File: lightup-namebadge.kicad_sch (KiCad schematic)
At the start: 22 parts, among them Q1 PNP, Q2 NPN, Q3 NPN, Q4 NPN, Q5 NPN, SW1 SW_Push, SW2 SW_Push

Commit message: fix: disconnect pin 3 of RV1 from VSS to save power
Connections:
- net VSS: no longer RV1.3
- no-connect marks 0 -> 1
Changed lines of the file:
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@@
-	)
-	(junction
-		(at 72.39 82.55)
-		(diameter 0)
-		(color 0 0 0 0)
 	)
 	(junction
@@
 	)
 	(junction
+		(at 135.89 92.71)
+		(diameter 0)
+		(color 0 0 0 0)
+	)
+	(junction
+		(at 153.67 82.55)
+		(diameter 0)
+		(color 0 0 0 0)
+	)
+	(junction
+		(at 196.85 90.17)
+		(diameter 0)
+		(color 0 0 0 0)
+	)
+	(junction
+		(at 176.53 90.17)
+		(diameter 0)
+		(color 0 0 0 0)
+	)
+	(junction
 		(at 107.95 121.92)
 		(diameter 0)
 		(color 0 0 0 0)
 	)
-	(junction
-		(at 135.89 92.71)
-		(diameter 0)
-		(color 0 0 0 0)
-	)
-	(junction
-		(at 153.67 82.55)
-		(diameter 0)
-		(color 0 0 0 0)
-	)
-	(junction
-		(at 196.85 90.17)
-		(diameter 0)
-		(color 0 0 0 0)
-	)
-	(junction
-		(at 176.53 90.17)
-		(diameter 0)
-		(color 0 0 0 0)
+	(no_connect
+		(at 88.9 82.55)
 	)
 	(wire
@@
 	(wire
 		(pts
-			(xy 72.39 82.55) (xy 72.39 71.12)
+			(xy 72.39 71.12) (xy 72.39 91.44)
 		)
 		(stroke
@@
 	(wire
 		(pts
+			(xy 100.33 93.98) (xy 111.76 93.98)
+		)
+		(stroke
+			(width 0)
+			(type default)
+		)
+	)
+	(wire
+		(pts
+			(xy 186.69 90.17) (xy 196.85 90.17)
+		)
+		(stroke
+			(width 0)
+			(type default)
+		)
+	)
+	(wire
+		(pts
+			(xy 176.53 97.79) (xy 186.69 97.79)
+		)
+		(stroke
+			(width 0)
+			(type default)
+		)
+	)
+	(wire
+		(pts
+			(xy 135.89 92.71) (xy 146.05 82.55)
+		)
+		(stroke
+			(width 0)
+			(type default)
+		)
+	)
+	(wire
+		(pts
+			(xy 135.89 96.52) (xy 135.89 92.71)
+		)
+		(stroke
+			(width 0)
+			(type default)
+		)
+	)
+	(wire
+		(pts
 			(xy 107.95 121.92) (xy 128.27 121.92)
 		)
@@
 	(wire
 		(pts
-			(xy 100.33 93.98) (xy 111.76 93.98)
-		)
-		(stroke
-			(width 0)
-			(type default)
-		)
-	)
-	(wire
-		(pts
-			(xy 186.69 90.17) (xy 196.85 90.17)
-		)
-		(stroke
-			(width 0)
-			(type default)
-		)
-	)
-	(wire
-		(pts
-			(xy 176.53 97.79) (xy 186.69 97.79)
-		)
-		(stroke
-			(width 0)
-			(type default)
-		)
-	)
-	(wire
-		(pts
-			(xy 135.89 92.71) (xy 146.05 82.55)
-		)
-		(stroke
-			(width 0)
-			(type default)
-		)
-	)
-	(wire
-		(pts
-			(xy 135.89 96.52) (xy 135.89 92.71)
-		)
-		(stroke
-			(width 0)
-			(type default)
-		)
-	)
-	(wire
-		(pts
 			(xy 207.01 97.79) (xy 218.44 97.79)
 		)
@@
 	(wire
 		(pts
-			(xy 72.39 82.55) (xy 88.9 82.55)
-		)
-		(stroke
-			(width 0)
-			(type default)
-		)
-	)
-	(wire
-		(pts
 			(xy 92.71 99.06) (xy 92.71 96.52)
 		)
@@
 		)
 		(stroke
-			(width 0)
-			(type default)
-		)
-	)
-	(wire
-		(pts
-			(xy 72.39 82.55) (xy 72.39 91.44)
-		)
-		(stroke

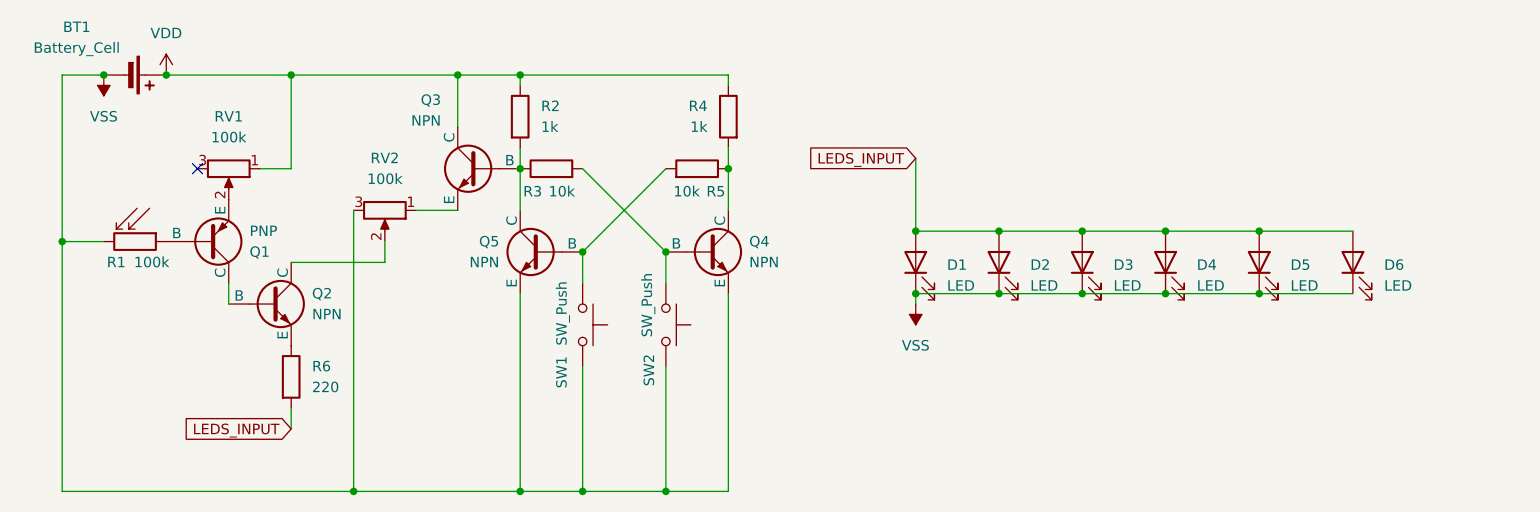
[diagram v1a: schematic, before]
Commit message: fix: new resistor values and more thermal relif for battery connector
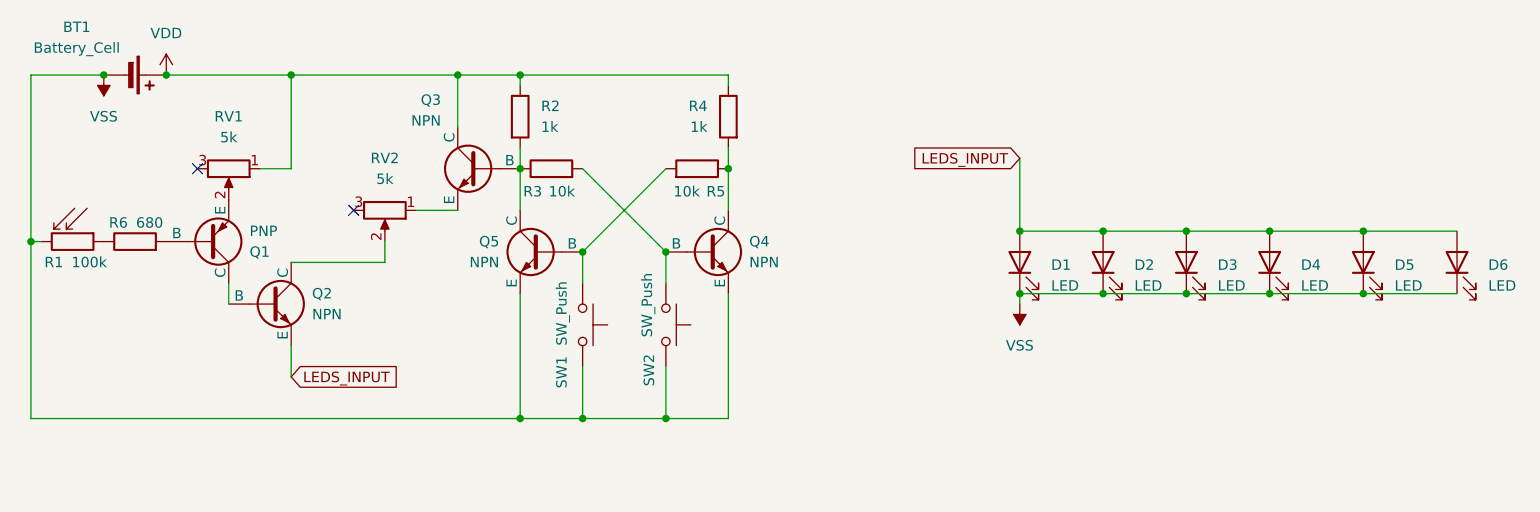
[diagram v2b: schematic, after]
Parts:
- R6: value 220 -> 680
- RV1, RV2: value 100k -> 5k
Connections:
- net LEDS_INPUT: now also Q2.3 (E); no longer R6.2
- net VSS: no longer RV2.3
- net at R6.1: now also R1.1; no longer Q2.3 (E)
- net at Q1.2 (B): now also R6.2; no longer R1.1
- no-connect marks 1 -> 2
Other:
- moved on the sheet: D1, D2, D3, D4, D5, D6, R1
